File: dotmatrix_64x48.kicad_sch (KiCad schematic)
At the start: 70 parts, among them J1 Conn_01x03_Female, J2 Conn_01x03_Male, J3 Micro_SD_Card, J7 Conn_01x04_Female, P1 CONN_01X06, Q2 Q_NPN_BEC, Q4 Q_NPN_BEC, SW1 SW_PUSH_SMALL_H, SW2 SW_PUSH_SMALL_H, U1 74VHC541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

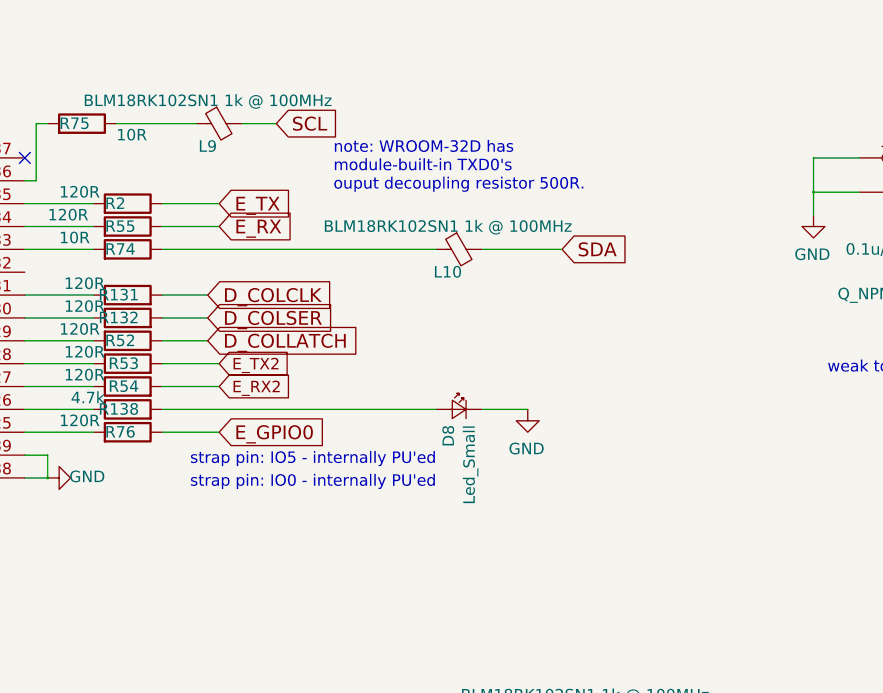
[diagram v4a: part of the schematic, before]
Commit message: Added some ferrite beads on sensitive lines
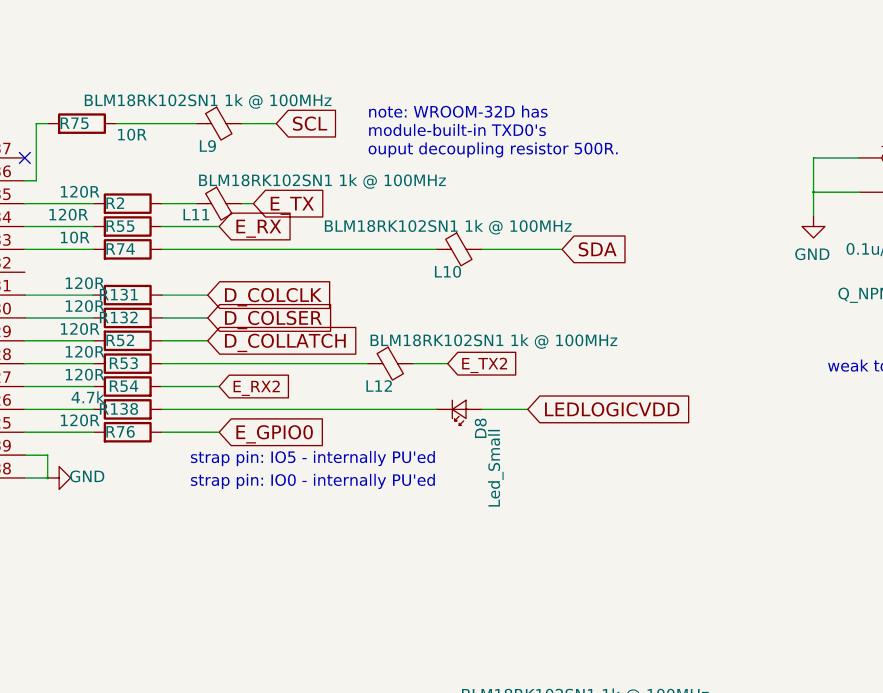
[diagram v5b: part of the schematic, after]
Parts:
- added L11, L12: BLM18RK102SN1 1k @ 100MHz, Resistor_SMD:R_0603_1608Metric_Pad1.05x0.95mm_HandSolder, symbol dotmatrix_64x48-rescue:Ferrite_Bead_Small-device
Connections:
- net E_TX: now also L11.2; no longer R2.1
- net E_TX2: now also L12.2; no longer R53.2
- net GND: no longer D8.1 (K)
- net LEDLOGICVDD: now also D8.2 (A)
- net at R138.2: now also D8.1 (K); no longer D8.2 (A)
- new net: L11.1, R2.1
- new net: L12.1, R53.2
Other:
- moved on the sheet: D8
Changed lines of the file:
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@@
   (junction (at 254 83.82) (diameter 0.3048) (color 0 0 0 0))
   (junction (at 259.08 34.29) (diameter 0.3048) (color 0 0 0 0))
+  (no_connect (at 125.73 27.94))
+  (no_connect (at 96.52 73.66))
   (no_connect (at 99.06 73.66))
   (no_connect (at 106.68 73.66))
-  (no_connect (at 125.73 27.94))
-  (no_connect (at 109.22 73.66))
-  (no_connect (at 96.52 73.66))
   (no_connect (at 101.6 73.66))
   (no_connect (at 151.13 137.16))
+  (no_connect (at 109.22 73.66))
+  (no_connect (at 48.26 87.63))
   (no_connect (at 104.14 73.66))
-  (no_connect (at 48.26 87.63))
   (wire (pts (xy 20.32 92.71) (xy 39.37 92.71))
     (stroke (width 0) (type solid) (color 0 0 0 0))
@@
     (stroke (width 0) (type solid) (color 0 0 0 0))
   )
-  (wire (pts (xy 140.97 33.02) (xy 147.32 33.02))
-    (stroke (width 0) (type solid) (color 0 0 0 0))
-  )
   (wire (pts (xy 140.97 35.56) (xy 147.32 35.56))
     (stroke (width 0) (type solid) (color 0 0 0 0))
@@
     (stroke (width 0) (type solid) (color 0 0 0 0))
   )
+  (wire (pts (xy 144.78 33.02) (xy 140.97 33.02))
+    (stroke (width 0) (type solid) (color 0 0 0 0))
+  )
   (wire (pts (xy 146.05 43.18) (xy 140.97 43.18))
     (stroke (width 0) (type solid) (color 0 0 0 0))
@@
     (stroke (width 0) (type solid) (color 0 0 0 0))
   )
-  (wire (pts (xy 147.32 50.8) (xy 140.97 50.8))
+  (wire (pts (xy 149.86 33.02) (xy 151.13 33.02))
     (stroke (width 0) (type solid) (color 0 0 0 0))
   )
@@
     (stroke (width 0) (type solid) (color 0 0 0 0))
   )
+  (wire (pts (xy 163.83 50.8) (xy 140.97 50.8))
+    (stroke (width 0) (type solid) (color 0 0 0 0))
+  )
   (wire (pts (xy 163.83 189.23) (xy 161.29 189.23))
     (stroke (width 0) (type solid) (color 0 0 0 0))
@@
   )
   (wire (pts (xy 171.45 90.17) (xy 181.61 90.17))
+    (stroke (width 0) (type solid) (color 0 0 0 0))
+  )
+  (wire (pts (xy 172.72 50.8) (xy 168.91 50.8))
     (stroke (width 0) (type solid) (color 0 0 0 0))
   )
@@
   )
   (text "note: WROOM-32D has \nmodule-built-in TXD0's \nouput decoupling resistor 500R."
-    (at 160.02 31.75 0)
+    (at 163.83 27.94 0)
     (effects (font (size 1.27 1.27)) (justify left bottom))
   )
@@
     (effects (font (size 1.524 1.524)) (justify left))
   )
-  (global_label "E_TX" (shape input) (at 147.32 33.02 0)
-    (effects (font (size 1.524 1.524)) (justify left))
-  )
   (global_label "E_RX" (shape input) (at 147.32 35.56 0)
     (effects (font (size 1.524 1.524)) (justify left))
   )
-  (global_label "E_TX2" (shape input) (at 147.32 50.8 0)
-    (effects (font (size 1.27 1.27)) (justify left))
-  )
   (global_label "E_RX2" (shape input) (at 147.32 53.34 0)
     (effects (font (size 1.27 1.27)) (justify left))
@@
     (effects (font (size 1.524 1.524)) (justify left))
   )
+  (global_label "E_TX" (shape input) (at 151.13 33.02 0)
+    (effects (font (size 1.524 1.524)) (justify left))
+  )
   (global_label "E_HS2_DATA0" (shape input) (at 151.13 132.08 0)
     (effects (font (size 1.27 1.27)) (justify left))
@@
   (global_label "LED1642VDD" (shape input) (at 171.45 90.17 180)
     (effects (font (size 1.524 1.524)) (justify right))
+  )
+  (global_label "E_TX2" (shape input) (at 172.72 50.8 0)
+    (effects (font (size 1.27 1.27)) (justify left))
+  )
+  (global_label "LEDLOGICVDD" (shape input) (at 181.61 55.88 0)
+    (effects (font (size 1.524 1.524)) (justify left))
   )
   (global_label "SDA" (shape input) (at 185.42 38.1 0)
@@
     (property "Datasheet" "" (id 3) (at 163.83 190.5 0))
   )
-  (symbol (lib_id "dotmatrix_64x48-rescue:GND-power") (at 181.61 55.88 0) (mirror y) (unit 1)
-    (in_bom yes) (on_board yes)
-    (property "Reference" "#PWR0153" (id 0) (at 181.61 62.23 0)
-      (effects (font (size 1.27 1.27)) hide)
-    )
-    (property "Value" "GND" (id 1) (at 181.483 60.2742 0))
-    (property "Footprint" "" (id 2) (at 181.61 55.88 0)
-      (effects (font (size 1.27 1.27)) hide)
-    )
-    (property "Datasheet" "" (id 3) (at 181.61 55.88 0)
-      (effects (font (size 1.27 1.27)) hide)
-    )
-  )
   (symbol (lib_id "dotmatrix_64x48-rescue:GND-power") (at 181.61 97.79 0) (unit 1)
     (in_bom yes) (on_board yes)
@@
     (property "Datasheet" "" (id 3) (at 269.24 34.29 0))
   )
-  (symbol (lib_id "dotmatrix_64x48-rescue:LED_Small-device") (at 173.99 55.88 0) (mirror y) (unit 1)
-    (in_bom yes) (on_board yes)
-    (property "Reference" "D8" (id 0) (at 172.8216 57.6072 90)
+  (symbol (lib_id "dotmatrix_64x48-rescue:LED_Small-device") (at 173.99 55.88 0) (mirror x) (unit 1)
+    (in_bom yes) (on_board yes)
+    (property "Reference" "D8" (id 0) (at 176.4284 59.2328 90)
       (effects (font (size 1.27 1.27)) (justify right))
     )
-    (property "Value" "Led_Small" (id 1) (at 175.133 57.6072 90)
+    (property "Value" "Led_Small" (id 1) (at 177.927 66.8528 90)
       (effects (font (size 1.27 1.27)) (justify right))
     )
@@
     )
     (property "Datasheet" "" (id 3) (at 147.32 24.13 0))
+  )
+  (symbol (lib_id "dotmatrix_64x48-rescue:Ferrite_Bead_Small-device") (at 147.32 33.02 90) (mirror x) (unit 1)
+    (in_bom yes) (on_board yes)
+    (property "Reference" "L11" (id 0) (at 144.78 34.29 90))
+    (property "Value" "BLM18RK102SN1 1k @ 100MHz" (id 1) (at 158.75 30.48 90))
+    (property "Footprint" "Resistor_SMD:R_0603_1608Metric_Pad1.05x0.95mm_HandSolder" (id 2) (at 147.32 33.02 0)
+      (effects (font (size 1.27 1.27)) hide)
+    )
+    (property "Datasheet" "" (id 3) (at 147.32 33.02 0))
+  )
+  (symbol (lib_id "dotmatrix_64x48-rescue:Ferrite_Bead_Small-device") (at 166.37 50.8 90) (mirror x) (unit 1)
+    (in_bom yes) (on_board yes)
+    (property "Reference" "L12" (id 0) (at 165.1 53.34 90))
+    (property "Value" "BLM18RK102SN1 1k @ 100MHz" (id 1) (at 177.8 48.26 90))
+    (property "Footprint" "Resistor_SMD:R_0603_1608Metric_Pad1.05x0.95mm_HandSolder" (id 2) (at 166.37 50.8 0)
+      (effects (font (size 1.27 1.27)) hide)
+    )
+    (property "Datasheet" "" (id 3) (at 166.37 50.8 0))
   )
   (symbol (lib_id "dotmatrix_64x48-rescue:Ferrite_Bead_Small-device") (at 173.99 38.1 90) (mirror x) (unit 1)
@@
       (reference "#PWR0142") (unit 1) (value "GND") (footprint "")
     )
-    (path "/00000000-0000-0000-0000-00005c0df9d3"
-      (reference "#PWR0153") (unit 1) (value "GND") (footprint "")
-    )
     (path "/00000000-0000-0000-0000-00005baee4a8"
       (reference "C21") (unit 1) (value "0.1u/35V") (footprint "Capacitor_SMD:C_0603_1608Metric_Pad1.05x0.95mm_HandSolder")
@@
       (reference "L10") (unit 1) (value "BLM18RK102SN1 1k @ 100MHz") (footprint "Resistor_SMD:R_0603_1608Metric_Pad1.05x0.95mm_HandSolder")
     )
+    (path "/43e0bb1c-a7db-4c69-b9da-02f45389f93f"
+      (reference "L11") (unit 1) (value "BLM18RK102SN1 1k @ 100MHz") (footprint "Resistor_SMD:R_0603_1608Metric_Pad1.05x0.95mm_HandSolder")
+    )
+    (path "/3d04eb01-8d4d-46b3-a39f-aa4bf964805e"
+      (reference "L12") (unit 1) (value "BLM18RK102SN1 1k @ 100MHz") (footprint "Resistor_SMD:R_0603_1608Metric_Pad1.05x0.95mm_HandSolder")
+    )
     (path "/00000000-0000-0000-0000-00005bb4df6a"

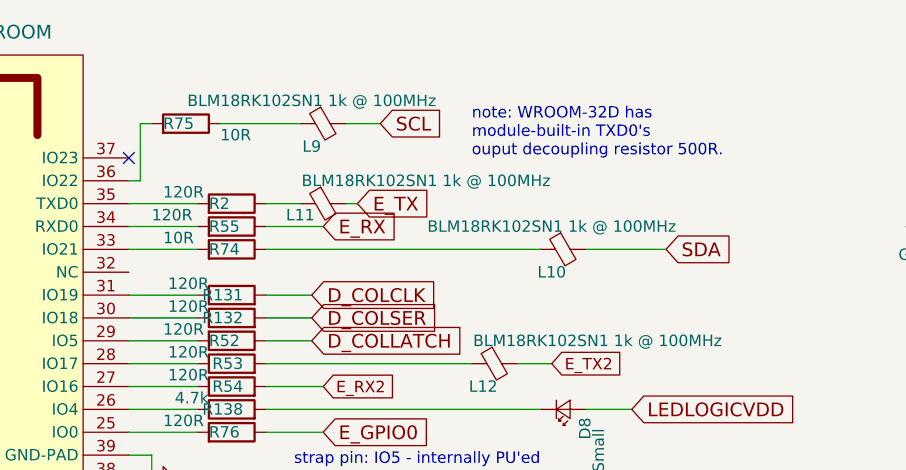
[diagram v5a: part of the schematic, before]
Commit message: Removed SCL/SDA FBs
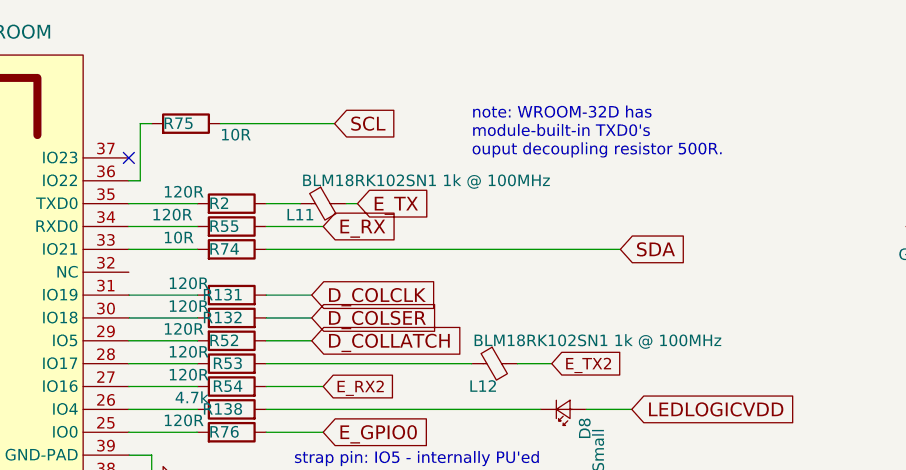
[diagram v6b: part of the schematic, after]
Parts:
- removed L10, L9: BLM18RK102SN1 1k @ 100MHz, Resistor_SMD:R_0603_1608Metric_Pad1.05x0.95mm_HandSolder, symbol dotmatrix_64x48-rescue:Ferrite_Bead_Small-device
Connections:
- net SCL: now also R75.1
- net SDA: now also R74.1
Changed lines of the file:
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@@
   (junction (at 254 83.82) (diameter 0.3048) (color 0 0 0 0))
   (junction (at 259.08 34.29) (diameter 0.3048) (color 0 0 0 0))
+  (no_connect (at 109.22 73.66))
   (no_connect (at 125.73 27.94))
+  (no_connect (at 99.06 73.66))
   (no_connect (at 96.52 73.66))
-  (no_connect (at 99.06 73.66))
   (no_connect (at 106.68 73.66))
+  (no_connect (at 104.14 73.66))
+  (no_connect (at 151.13 137.16))
   (no_connect (at 101.6 73.66))
-  (no_connect (at 151.13 137.16))
-  (no_connect (at 109.22 73.66))
   (no_connect (at 48.26 87.63))
-  (no_connect (at 104.14 73.66))
   (wire (pts (xy 20.32 92.71) (xy 39.37 92.71))
     (stroke (width 0) (type solid) (color 0 0 0 0))
@@
     (stroke (width 0) (type solid) (color 0 0 0 0))
   )
+  (wire (pts (xy 135.89 24.13) (xy 148.59 24.13))
+    (stroke (width 0) (type solid) (color 0 0 0 0))
+  )
   (wire (pts (xy 140.97 35.56) (xy 147.32 35.56))
     (stroke (width 0) (type solid) (color 0 0 0 0))
   )
-  (wire (pts (xy 140.97 38.1) (xy 171.45 38.1))
+  (wire (pts (xy 140.97 38.1) (xy 180.34 38.1))
     (stroke (width 0) (type solid) (color 0 0 0 0))
   )
@@
     (stroke (width 0) (type solid) (color 0 0 0 0))
   )
-  (wire (pts (xy 144.78 24.13) (xy 135.89 24.13))
-    (stroke (width 0) (type solid) (color 0 0 0 0))
-  )
   (wire (pts (xy 144.78 33.02) (xy 140.97 33.02))
     (stroke (width 0) (type solid) (color 0 0 0 0))
@@
     (stroke (width 0) (type solid) (color 0 0 0 0))
   )
-  (wire (pts (xy 153.67 24.13) (xy 149.86 24.13))
-    (stroke (width 0) (type solid) (color 0 0 0 0))
-  )
   (wire (pts (xy 163.83 50.8) (xy 140.97 50.8))
     (stroke (width 0) (type solid) (color 0 0 0 0))
@@
   )
   (wire (pts (xy 172.72 50.8) (xy 168.91 50.8))
-    (stroke (width 0) (type solid) (color 0 0 0 0))
-  )
-  (wire (pts (xy 176.53 38.1) (xy 185.42 38.1))
     (stroke (width 0) (type solid) (color 0 0 0 0))
   )
@@
     (effects (font (size 1.524 1.524)) (justify left))
   )
+  (global_label "SCL" (shape input) (at 148.59 24.13 0)
+    (effects (font (size 1.524 1.524)) (justify left))
+  )
   (global_label "E_TX" (shape input) (at 151.13 33.02 0)
     (effects (font (size 1.524 1.524)) (justify left))
@@
     (effects (font (size 1.27 1.27)) (justify left))
   )
-  (global_label "SCL" (shape input) (at 153.67 24.13 0)
-    (effects (font (size 1.524 1.524)) (justify left))
-  )
   (global_label "LED1642VDD" (shape input) (at 171.45 90.17 180)
     (effects (font (size 1.524 1.524)) (justify right))
@@
     (effects (font (size 1.27 1.27)) (justify left))
   )
+  (global_label "SDA" (shape input) (at 180.34 38.1 0)
+    (effects (font (size 1.524 1.524)) (justify left))
+  )
   (global_label "LEDLOGICVDD" (shape input) (at 181.61 55.88 0)
-    (effects (font (size 1.524 1.524)) (justify left))
-  )
-  (global_label "SDA" (shape input) (at 185.42 38.1 0)
     (effects (font (size 1.524 1.524)) (justify left))
   )
@@
     (property "Datasheet" "" (id 3) (at 100.33 173.99 0))
   )
-  (symbol (lib_id "dotmatrix_64x48-rescue:Ferrite_Bead_Small-device") (at 147.32 24.13 90) (mirror x) (unit 1)
-    (in_bom yes) (on_board yes)
-    (property "Reference" "L9" (id 0) (at 146.05 26.67 90))
-    (property "Value" "BLM18RK102SN1 1k @ 100MHz" (id 1) (at 146.05 21.59 90))
-    (property "Footprint" "Resistor_SMD:R_0603_1608Metric_Pad1.05x0.95mm_HandSolder" (id 2) (at 147.32 24.13 0)
-      (effects (font (size 1.27 1.27)) hide)
-    )
-    (property "Datasheet" "" (id 3) (at 147.32 24.13 0))
-  )
   (symbol (lib_id "dotmatrix_64x48-rescue:Ferrite_Bead_Small-device") (at 147.32 33.02 90) (mirror x) (unit 1)
     (in_bom yes) (on_board yes)
@@
     )
     (property "Datasheet" "" (id 3) (at 166.37 50.8 0))
-  )
-  (symbol (lib_id "dotmatrix_64x48-rescue:Ferrite_Bead_Small-device") (at 173.99 38.1 90) (mirror x) (unit 1)
-    (in_bom yes) (on_board yes)
-    (property "Reference" "L10" (id 0) (at 172.72 40.64 90))
-    (property "Value" "BLM18RK102SN1 1k @ 100MHz" (id 1) (at 172.72 35.56 90))
-    (property "Footprint" "Resistor_SMD:R_0603_1608Metric_Pad1.05x0.95mm_HandSolder" (id 2) (at 173.99 38.1 0)
-      (effects (font (size 1.27 1.27)) hide)
-    )
-    (property "Datasheet" "" (id 3) (at 173.99 38.1 0))
   )
   (symbol (lib_id "dotmatrix_64x48-rescue:Ferrite_Bead_Small-device") (at 189.23 90.17 90) (mirror x) (unit 1)
@@
       (reference "L5") (unit 1) (value "BLM21PG331SN 300R@100MHz") (footprint "Capacitors_SMD:C_0805_HandSoldering")
     )
-    (path "/c788adc5-bd1b-4179-9658-5ebe5800a5bd"
-      (reference "L9") (unit 1) (value "BLM18RK102SN1 1k @ 100MHz") (footprint "Resistor_SMD:R_0603_1608Metric_Pad1.05x0.95mm_HandSolder")
-    )
-    (path "/9e0326f7-50f2-4702-8dfc-880eee015938"
-      (reference "L10") (unit 1) (value "BLM18RK102SN1 1k @ 100MHz") (footprint "Resistor_SMD:R_0603_1608Metric_Pad1.05x0.95mm_HandSolder")
-    )
     (path "/43e0bb1c-a7db-4c69-b9da-02f45389f93f"

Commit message: Moved leftside sensors to rightside; Unified old footprints to new footprints; DRC clear
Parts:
- L3: footprint Resistors_SMD:R_0603_HandSoldering -> Resistor_SMD:R_0603_1608Metric_Pad1.05x0.95mm_HandSolder
- L5: footprint Capacitors_SMD:C_0805_HandSoldering -> Capacitor_SMD:C_0805_2012Metric_Pad1.15x1.40mm_HandSolder
